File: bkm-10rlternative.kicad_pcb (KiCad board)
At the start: 4 copper layers, 210.8 x 74.9 mm, 234 parts, among them J1 DB9_Male_MountingHoles, Q1 MMBT3904, Q10 MMBT3904, Q11 MMBT3904, Q12 MMBT3904, Q13 MMBT3904, Q14 MMBT3904, Q2 MMBT3904, Q3 MMBT3904, Q4 MMBT3904, Q5 MMBT3904, Q6 MMBT3904, Q7 MMBT3904, Q8 MMBT3904, Q9 MMBT3904, SW1 SHIFT, SW10 ADDR_SAFE_AREA, SW11 UP, SW12 MENU, SW13 DOWN, SW14 ENTER, SW15 DEGAUSS, SW16 POWER, SW17 KEY_1, SW18 KEY_2, SW19 KEY_3, SW2 HORIZ_SYNC, SW20 KEY_4, SW21 KEY_5, SW22 KEY_6, SW23 KEY_7, SW24 KEY_8, SW25 KEY_9, SW26 KEY_DEL, SW27 KEY_0, SW28 KEY_ENTER, SW29 CONTRAST_MANUAL, SW3 UNDERSCAN_16_9, SW30 CONTRAST_KNOB, SW31 BRIGHT_MANUAL, SW32 BRIGHT_KNOB, SW33 CHROMA_MANUAL, SW34 CHROMA_KNOB, SW35 PHASE_MANUAL, SW36 PHASE_KNOB, SW4 VERT_BLUE_ONLY, SW5 MONO_R, SW6 APT_G, SW7 COMB_B, SW8 F1_F3, SW9 F2_F4, U1 74LVC2G14, U10 MCP23S17_SS, U11 MCP23S17_SS, U12 MCP23S17_SS, U13 74LVC2G14, U14 74LVC2G14, U15 74LVC2G14, U16 74LVC2G14, U17 74LVC2G14, U18 74LVC2G14, U19 74LVC2G14, U2 74HC14, U20 74LVC2G14, U3 74HC14, U4 74HC14, U5 74HC14, U6 TSOP382xx, U8 MAX485E, U9 ATmega328PB-AU, Y1 Resonator

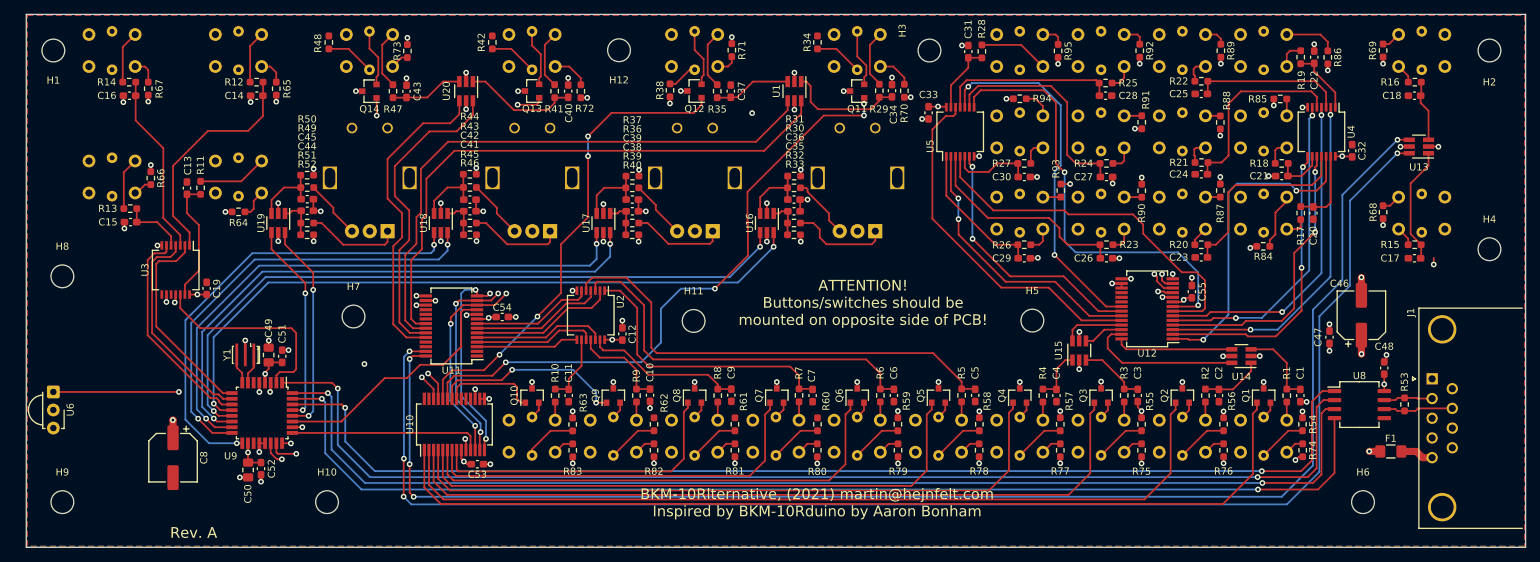
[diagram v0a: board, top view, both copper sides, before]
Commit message: Added texts, fixed pullups
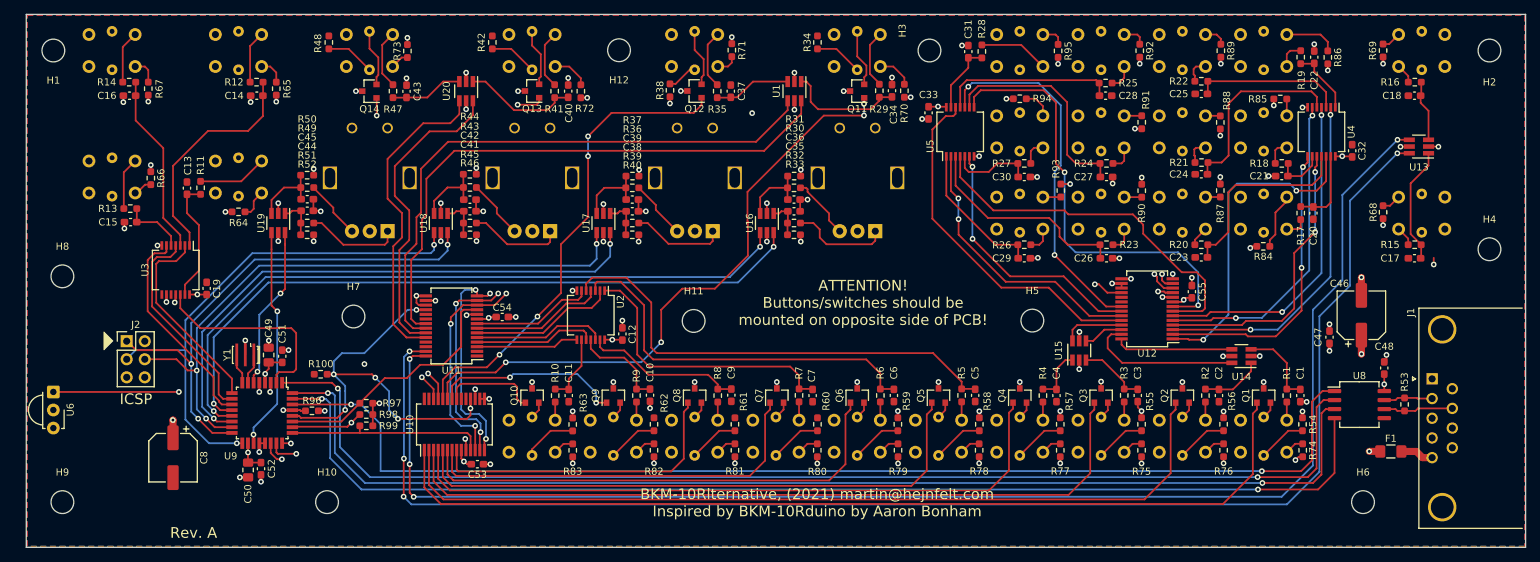
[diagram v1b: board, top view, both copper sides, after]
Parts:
- added J2: ICSP, Connector_PinHeader_2.54mm:PinHeader_2x03_P2.54mm_Vertical, F.Cu at (58.6, 77.7)
- added R100: 10K, Resistor_SMD:R_0603_1608Metric_Pad0.98x0.95mm_HandSolder, F.Cu at (85.9, 82.3)
- added R96: 10K, Resistor_SMD:R_0603_1608Metric_Pad0.98x0.95mm_HandSolder, F.Cu at (84.6, 87.5)
- added R97: 10K, Resistor_SMD:R_0603_1608Metric_Pad0.98x0.95mm_HandSolder, F.Cu at (92.3, 86.4)
- added R98: 10K, Resistor_SMD:R_0603_1608Metric_Pad0.98x0.95mm_HandSolder, F.Cu at (92.3, 88.0)
- added R99: 10K, Resistor_SMD:R_0603_1608Metric_Pad0.98x0.95mm_HandSolder, F.Cu at (92.3, 89.6)
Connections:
- net /MCU+RS485/IR_OUT renamed /MCU+RS485/IR_IN
- U10 pad 18: (no net) -> ~GPIO_RESET
- U11 pad 18: (no net) -> ~GPIO_RESET
- U12 pad 18: (no net) -> ~GPIO_RESET
- U9 pad 19: (no net) -> PHASE_B
- U9 pad 28: PHASE_A -> ~GPIO_RESET
- U9 pad 29: PHASE_B -> MCU_RESET
- U9 pad 6: (no net) -> PHASE_A
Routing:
- net ~GPIO_RESET: track 0.00 -> 157.8 mm, vias 0 -> 7
- net MCU_RESET: track 0.00 -> 27.1 mm, vias 0 -> 1
- net CHROMA_A: track 62.2 -> 72.6 mm, vias 2 -> 3
- net CHROMA_B: track 64.9 -> 73.7 mm
- net BRIGHT_B: track 81.4 -> 89.3 mm, vias 2 -> 3
- net PHASE_A: track 30.0 -> 23.5 mm
- net VCC: track 104.6 -> 109.6 mm, vias 81 -> 83
- net PHASE_B: track 28.5 -> 31.3 mm
- net SS1: track 133.3 -> 134.9 mm
- net SCK: track 153.6 -> 154.8 mm
- net GND: track 80.7 -> 81.8 mm, vias 66 -> 65
- net MISO: track 159.4 -> 160.5 mm
- net UART0_RXD: track 162.7 -> 163.8 mm
- net MOSI: track 159.3 -> 160.3 mm
- net SS2: track 27.2 -> 28.2 mm
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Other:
- board text added: "0"
- board text added: "1"
- board text added: "16:9"
- board text added: "2"
- board text added: "3"
- board text added: "4"
- board text added: "5"
- board text added: "6"
- board text added: "7"
- board text added: "8"
- board text added: "9"
- board text added: "ADDRESS"
- board text added: "APT"
- board text added: "B"
- board text added: "BLUE ONLY"
- board text added: "BRIGHT"
- board text added: "CHROMA"
- board text added: "COMB"
- board text added: "CONTRAST"
- board text added: "DEGAUSS"
- board text added: "DEL"
- board text added: "DOWN"
- board text added: "ENT"
- board text added: "ENTER"
- board text added: "F1"
- board text added: "F2"
- board text added: "F3"
- board text added: "F4"
- board text added: "G"
- board text added: "ICSP"
- board text added: "MANUAL"
- board text added: "MENU"
- board text added: "MONO"
- board text added: "PHASE"
- board text added: "POWER"
- board text added: "R"
- board text added: "SAFE AREA"
- board text added: "SHIFT"
- board text added: "SYNC"
- board text added: "UP"

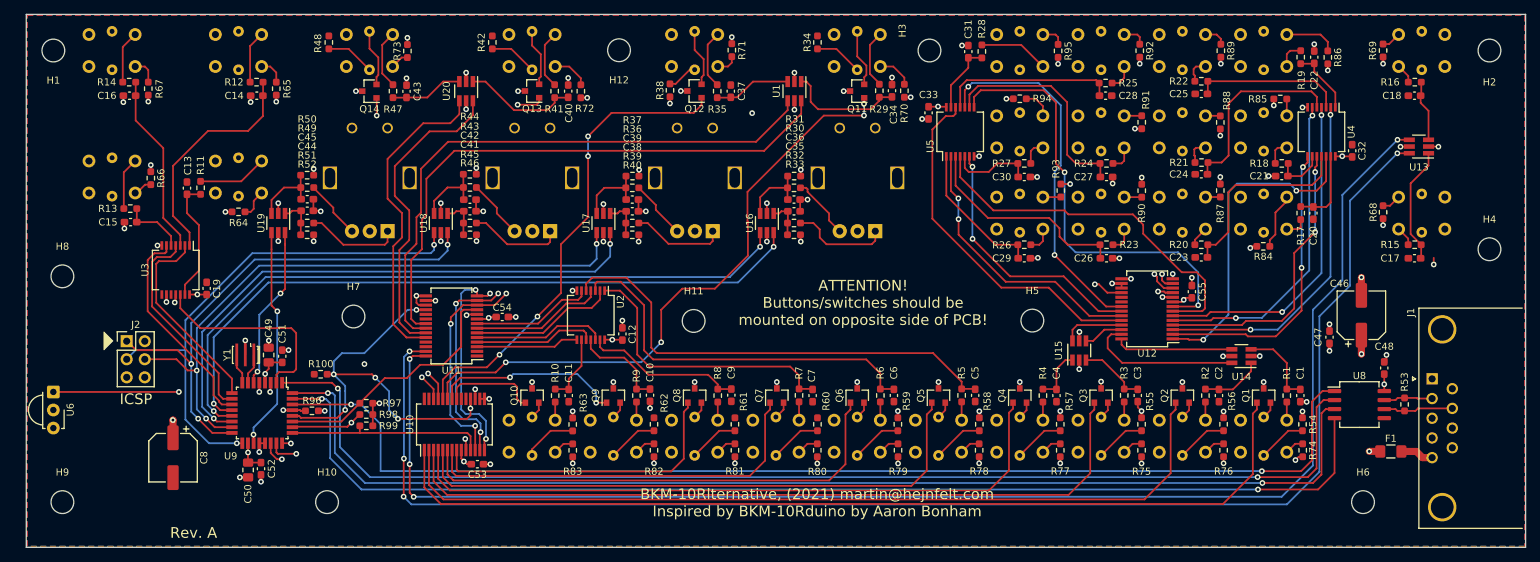
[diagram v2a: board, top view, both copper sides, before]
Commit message: A bunch of changes, full duplex 422
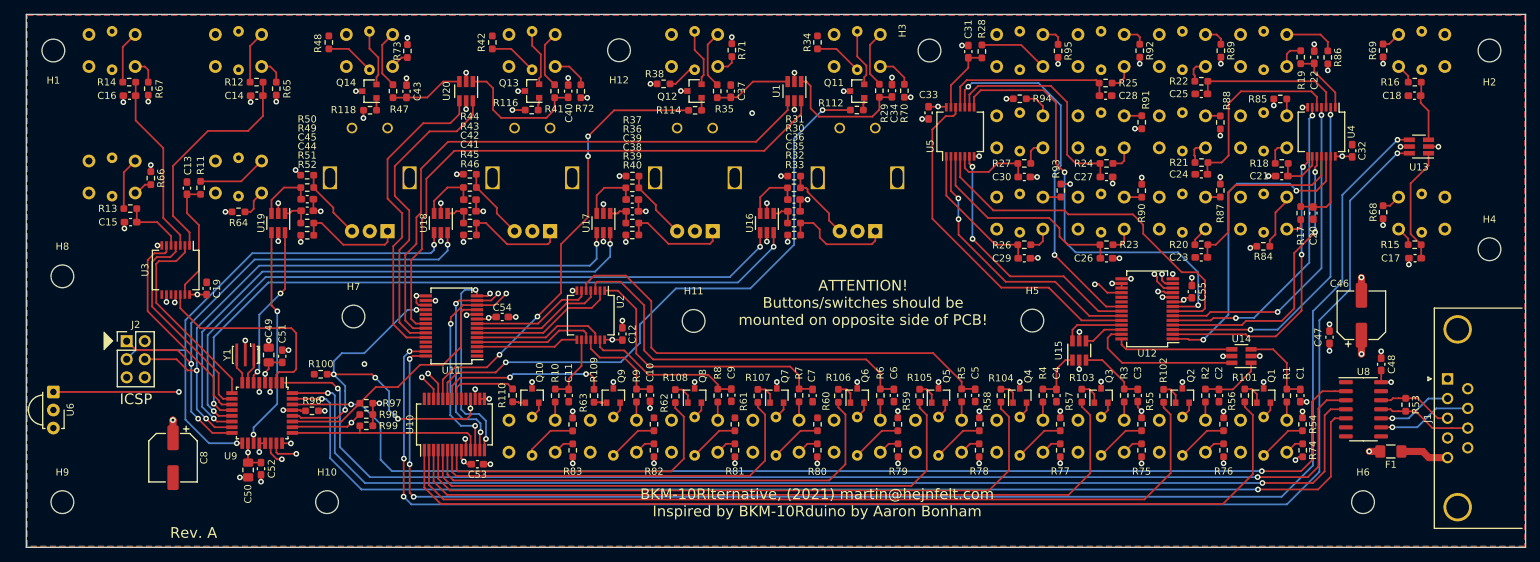
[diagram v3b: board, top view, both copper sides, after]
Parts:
- added R101: 560R, Resistor_SMD:R_0603_1608Metric_Pad0.98x0.95mm_HandSolder, F.Cu at (215.8, 85.3)
- added R102: 560R, Resistor_SMD:R_0603_1608Metric_Pad0.98x0.95mm_HandSolder, F.Cu at (204.4, 85.4)
- added R103: 560R, Resistor_SMD:R_0603_1608Metric_Pad0.98x0.95mm_HandSolder, F.Cu at (192.9, 85.4)
- added R104: 560R, Resistor_SMD:R_0603_1608Metric_Pad0.98x0.95mm_HandSolder, F.Cu at (181.5, 85.4)
- added R105: 560R, Resistor_SMD:R_0603_1608Metric_Pad0.98x0.95mm_HandSolder, F.Cu at (170.1, 85.4)
- added R106: 560R, Resistor_SMD:R_0603_1608Metric_Pad0.98x0.95mm_HandSolder, F.Cu at (158.6, 85.4)
- added R107: 560R, Resistor_SMD:R_0603_1608Metric_Pad0.98x0.95mm_HandSolder, F.Cu at (147.3, 85.4)
- added R108: 560R, Resistor_SMD:R_0603_1608Metric_Pad0.98x0.95mm_HandSolder, F.Cu at (135.7, 85.4)
- added R109: 560R, Resistor_SMD:R_0603_1608Metric_Pad0.98x0.95mm_HandSolder, F.Cu at (124.3, 85.4)
- added R110: 560R, Resistor_SMD:R_0603_1608Metric_Pad0.98x0.95mm_HandSolder, F.Cu at (112.8, 85.3)
- added R112: 560R, Resistor_SMD:R_0603_1608Metric_Pad0.98x0.95mm_HandSolder, F.Cu at (161.2, 45.2)
- added R114: 560R, Resistor_SMD:R_0603_1608Metric_Pad0.98x0.95mm_HandSolder, F.Cu at (138.5, 45.2)
- added R116: 560R, Resistor_SMD:R_0603_1608Metric_Pad0.98x0.95mm_HandSolder, F.Cu at (115.5, 45.2)
- added R118: 560R, Resistor_SMD:R_0603_1608Metric_Pad0.98x0.95mm_HandSolder, F.Cu at (92.8, 45.2)
- J1: footprint Connector_Dsub:DSUB-9_Female_Horizontal_P2.77x2.84mm_EdgePinOffset9.90mm_Housed_MountingHolesOffset11.32mm -> Connector_Dsub:DSUB-9_Female_Horizontal_P2.77x2.84mm_EdgePinOffset7.70mm_Housed_MountingHolesOffset9.12mm
- U8: value MAX485E -> MAX491E; footprint Package_SO:SO-8_5.3x6.2mm_P1.27mm -> Package_SO:SOIC-14_3.9x8.7mm_P1.27mm
- moved J1 2.17 mm to (244.3, 83.0)
- moved R38 1.28 mm to (134.1, 41.5), turned to 180 degrees
- moved U8 0.87 mm to (232.5, 87.3)
- moved C48 0.68 mm to (235.0, 80.9)
- moved R53 0.16 mm to (238.4, 86.6)
- moved C17 0.08 mm to (239.7, 66.0)
- moved R52 0.06 mm to (84.0, 62.8), turned to 180 degrees
- turned R33 to 180 degrees
- turned R40 to 180 degrees
- turned R46 to 180 degrees
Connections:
- J1 pad 2: RS485_B -> /MCU+RS485/~TXD
- J1 pad 3: (no net) -> /MCU+RS485/RXD
- J1 pad 7: RS485_A -> /MCU+RS485/TXD
- J1 pad 8: (no net) -> /MCU+RS485/~RXD
- Q1 pad 1: SHIFT_ACTIVE_LED -> Net-(Q1-Pad1)
- Q10 pad 1: ADDR_SAFE_AREA_ACTIVE_LED -> Net-(Q10-Pad1)
- Q11 pad 1: CONTRAST_MANUAL_ACTIVE_LED -> Net-(Q11-Pad1)
- Q12 pad 1: BRIGHT_MANUAL_ACTIVE_LED -> Net-(Q12-Pad1)
- Q13 pad 1: CHROMA_MANUAL_ACTIVE_LED -> Net-(Q13-Pad1)
- Q14 pad 1: PHASE_MANUAL_ACTIVE_LED -> Net-(Q14-Pad1)
- Q2 pad 1: UNDERSCAN_16_9_ACTIVE_LED -> Net-(Q2-Pad1)
- Q3 pad 1: HORIZ_SYNC_ACTIVE_LED -> Net-(Q3-Pad1)
- Q4 pad 1: VERT_BLUE_ONLY_ACTIVE_LED -> Net-(Q4-Pad1)
- Q5 pad 1: MONO_R_ACTIVE_LED -> Net-(Q5-Pad1)
- Q6 pad 1: APT_G_ACTIVE_LED -> Net-(Q6-Pad1)
- Q7 pad 1: COMB_B_ACTIVE_LED -> Net-(Q7-Pad1)
- Q8 pad 1: F1_F3_ACTIVE_LED -> Net-(Q8-Pad1)
- Q9 pad 1: F2_F4_ACTIVE_LED -> Net-(Q9-Pad1)
- R31 pad 1: VCC -> Net-(R30-Pad2)
- R31 pad 2: Net-(C36-Pad1) -> VCC
- R33 pad 1: Net-(C35-Pad2) -> Net-(R32-Pad1)
- R37 pad 1: VCC -> Net-(R36-Pad2)
- R37 pad 2: Net-(C39-Pad1) -> VCC
- R40 pad 1: Net-(C38-Pad2) -> Net-(R39-Pad1)
- R44 pad 1: VCC -> Net-(R43-Pad2)
- R44 pad 2: Net-(C42-Pad1) -> VCC
- R46 pad 1: Net-(C41-Pad2) -> Net-(R45-Pad1)
- R50 pad 1: VCC -> Net-(R49-Pad2)
- R50 pad 2: Net-(C45-Pad1) -> VCC
- R52 pad 1: Net-(C44-Pad2) -> Net-(R51-Pad1)
- R53 pad 1: RS485_B -> /MCU+RS485/RXD
- R53 pad 2: RS485_A -> /MCU+RS485/~RXD
- U8 pad 1: UART0_RXD -> (no net)
- U8 pad 2: UART_CTS -> UART0_RXD
- U8 pad 3: UART_RTS -> UART_CTS
- U8 pad 4: UART0_TXD -> UART_RTS
- U8 pad 5: GND -> UART0_TXD
- U8 pad 6: RS485_A -> GND
- U8 pad 7: RS485_B -> GND
- U8 pad 8: VCC -> (no net)
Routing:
- net /MCU+RS485/TXD: track 0.00 -> 13.3 mm, vias 0 -> 1
- net /MCU+RS485/~RXD: track 0.00 -> 13.3 mm
- net /MCU+RS485/RXD: track 0.00 -> 10.6 mm
- net /MCU+RS485/~TXD: track 0.00 -> 10.5 mm, vias 0 -> 1
- net RS485_A: track 9.82 -> 0.00 mm
- net RS485_B: track 6.88 -> 0.00 mm
- net ADDR_SAFE_AREA_ACTIVE_LED: track 13.5 -> 9.95 mm
- net Net-(Q4-Pad1): track 0.00 -> 3.31 mm
- net Net-(Q3-Pad1): track 0.00 -> 3.26 mm
- net Net-(Q6-Pad1): track 0.00 -> 3.25 mm
- net Net-(C40-Pad1): track 16.2 -> 19.5 mm
- net Net-(Q1-Pad1): track 0.00 -> 3.20 mm
- net Net-(Q7-Pad1): track 0.00 -> 3.19 mm
- net Net-(Q5-Pad1): track 0.00 -> 3.17 mm
- net BRIGHT_MANUAL_ACTIVE_LED: track 66.8 -> 63.7 mm
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
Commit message: Fixed switch footprints and encoder resistors
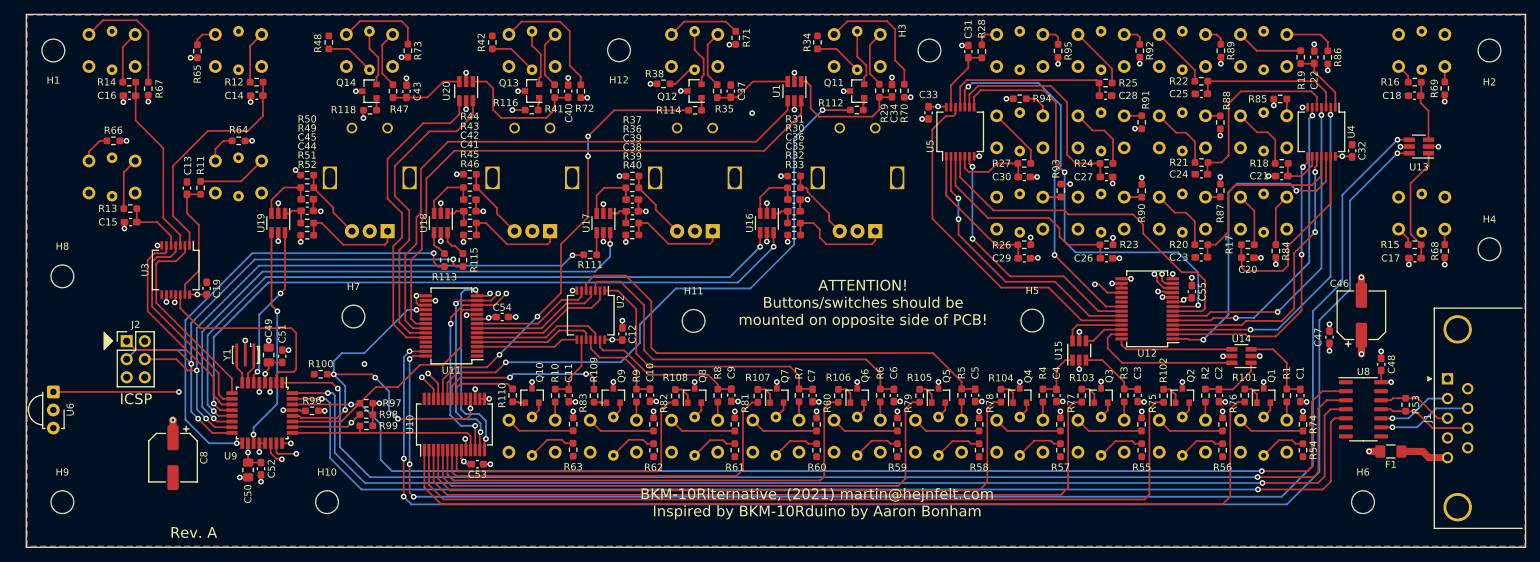
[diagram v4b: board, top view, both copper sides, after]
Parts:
- added R111: 1K, Resistor_SMD:R_0603_1608Metric_Pad0.98x0.95mm_HandSolder, F.Cu at (123.8, 65.5)
- added R113: 1K, Resistor_SMD:R_0603_1608Metric_Pad0.98x0.95mm_HandSolder, F.Cu at (103.3, 66.3)
- added R115: 1K, Resistor_SMD:R_0603_1608Metric_Pad0.98x0.95mm_HandSolder, F.Cu at (105.8, 66.3)
- R53: value 100R -> NM
- moved R65 12.3 mm to (68.5, 36.9)
- moved C20 11.1 mm to (216.2, 66.0), turned to 0 degrees
- moved R68 10.3 mm to (243.9, 65.0)
- moved R69 10.2 mm to (243.9, 42.2)
- moved R64 9.98 mm to (74.3, 49.5), turned to 0 degrees
- moved R17 8.66 mm to (216.2, 64.1), turned to 0 degrees
- moved R66 7.43 mm to (56.7, 49.5), turned to 0 degrees
- moved R83 3.67 mm to (121.3, 89.4), turned to 90 degrees
- moved R56 3.65 mm to (212.7, 93.0), turned to 270 degrees
- moved R60 3.65 mm to (155.6, 93.0), turned to 270 degrees
- moved R54 3.65 mm to (224.0, 93.0), turned to 270 degrees
- moved R59 3.65 mm to (166.9, 93.0), turned to 270 degrees
- moved R62 3.65 mm to (132.7, 93.0), turned to 270 degrees
- moved R55 3.64 mm to (201.3, 93.0), turned to 270 degrees
- moved R57 3.64 mm to (189.9, 93.0), turned to 270 degrees
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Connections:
- U17 pad 4: BRIGHT_B -> Net-(R111-Pad2)
- U18 pad 4: CHROMA_B -> Net-(R113-Pad2)
- U18 pad 6: CHROMA_A -> Net-(R115-Pad2)
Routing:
- net Net-(C20-Pad1): track 11.0 -> 28.1 mm
- net Net-(R67-Pad1): track 3.76 -> 17.0 mm
- net Net-(R70-Pad1): track 4.96 -> 18.1 mm
- net Net-(R72-Pad1): track 5.72 -> 18.0 mm
- net Net-(R73-Pad1): track 2.61 -> 12.1 mm
- net Net-(R71-Pad1): track 3.05 -> 10.4 mm
- net Net-(R20-Pad2): track 2.81 -> 9.69 mm
- net Net-(R83-Pad1): track 2.96 -> 9.65 mm
- net Net-(R74-Pad1): track 2.73 -> 9.40 mm
- net Net-(R77-Pad1): track 2.93 -> 9.60 mm
- net Net-(R78-Pad1): track 2.95 -> 9.60 mm
- net Net-(R75-Pad1): track 2.93 -> 9.57 mm
- net Net-(R81-Pad1): track 2.90 -> 9.54 mm
- net Net-(R23-Pad2): track 3.47 -> 10.1 mm, vias 0 -> 1
- net Net-(R82-Pad1): track 2.95 -> 9.54 mm
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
